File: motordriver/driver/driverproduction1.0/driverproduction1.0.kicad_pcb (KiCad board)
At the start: 4 copper layers, 28 parts

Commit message: l
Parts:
- added REF**: R_Axial_DIN0204_L3.6mm_D1.6mm_P5.08mm_Vertical, Resistor_THT:R_Axial_DIN0204_L3.6mm_D1.6mm_P5.08mm_Vertical, F.Cu at (58.7, 45.0)
- added REF**: C_Disc_D8.0mm_W5.0mm_P7.50mm, Capacitor_THT:C_Disc_D8.0mm_W5.0mm_P7.50mm, F.Cu at (73.0, 62.8)
- added REF**: C_Rect_L11.5mm_W7.8mm_P10.00mm_MKT, Capacitor_THT:C_Rect_L11.5mm_W7.8mm_P10.00mm_MKT, F.Cu at (50.6, 37.0)
- added REF**: Choke_Schaffner_RN216-04-15.5x23.0mm, Inductor_THT:Choke_Schaffner_RN216-04-15.5x23.0mm, F.Cu at (61.5, 49.8)
- added REF**: C_Radial_D16.0mm_H25.0mm_P7.50mm, Capacitor_THT:C_Radial_D16.0mm_H25.0mm_P7.50mm, F.Cu at (159.0, 43.8)
- added REF**: D_0603_1608Metric_Pad1.05x0.95mm_HandSolder, Diode_SMD:D_0603_1608Metric_Pad1.05x0.95mm_HandSolder, F.Cu at (152.5, 48.0)
- added REF**: C_Disc_D8.0mm_W5.0mm_P7.50mm, Capacitor_THT:C_Disc_D8.0mm_W5.0mm_P7.50mm, F.Cu at (73.0, 80.5)
- added REF**: D_0603_1608Metric_Pad1.05x0.95mm_HandSolder, Diode_SMD:D_0603_1608Metric_Pad1.05x0.95mm_HandSolder, F.Cu at (152.5, 57.5)
- added REF**: C_Radial_D16.0mm_H25.0mm_P7.50mm, Capacitor_THT:C_Radial_D16.0mm_H25.0mm_P7.50mm, F.Cu at (159.0, 61.8)
- moved Q** 78.4 mm to (40.6, 80.1), turned to 180 degrees
- moved Q** 77.7 mm to (40.5, 107.4), turned to 0 degrees
- moved Q** 76.6 mm to (40.6, 85.6), turned to 0 degrees
- moved Q** 76.4 mm to (40.5, 102.0), turned to 180 degrees
- moved Q** 75.7 mm to (40.6, 91.1), turned to 180 degrees
- moved Q** 75.5 mm to (40.6, 96.5), turned to 0 degrees
- moved REF** 69.5 mm to (44.9, 96.4), turned to 0 degrees
- moved REF** 69.5 mm to (44.9, 95.5), turned to 0 degrees
- moved REF** 69.1 mm to (45.2, 93.0), turned to 0 degrees
- moved REF** 69.0 mm to (45.2, 93.9), turned to 0 degrees
- moved REF** 68.7 mm to (46.3, 85.9), turned to -45 degrees
- moved REF** 68.0 mm to (46.9, 85.3), turned to -45 degrees
- moved REF** 68.0 mm to (46.6, 102.8), turned to 45 degrees
- moved REF** 67.6 mm to (47.3, 84.5), turned to -45 degrees
- moved REF** 67.4 mm to (46.5, 90.5), turned to 135 degrees
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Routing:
- net (no net): track 251.1 -> 420.2 mm
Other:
- board outline added: 180 x 100 mm

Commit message: esp32 routin
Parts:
- added REF**: C_0402_1005Metric, Capacitor_SMD:C_0402_1005Metric, F.Cu at (176.2, 83.4)
- added REF**: QFN56_7X7_EXP, esp32-s3:QFN56_7X7_EXP-L, F.Cu at (182.9, 91.4)
- added REF**: C_0402_1005Metric, Capacitor_SMD:C_0402_1005Metric, F.Cu at (179.0, 84.8)
- added REF**: C_0402_1005Metric, Capacitor_SMD:C_0402_1005Metric, F.Cu at (179.1, 83.4)
- added REF**: C_0402_1005Metric, Capacitor_SMD:C_0402_1005Metric, F.Cu at (176.7, 89.0)
- added REF**: L_0402_1005Metric, Inductor_SMD:L_0402_1005Metric, F.Cu at (176.3, 87.1)
- added REF**: C_0402_1005Metric, Capacitor_SMD:C_0402_1005Metric, F.Cu at (176.2, 84.8)
- added REF**: SOIC-8-1EP_3.9x4.9mm_P1.27mm_EP2.29x3mm, Package_SO:SOIC-8-1EP_3.9x4.9mm_P1.27mm_EP2.29x3mm, F.Cu at (196.4, 94.8)
- added REF**: C_0402_1005Metric, Capacitor_SMD:C_0402_1005Metric, F.Cu at (174.4, 86.8)
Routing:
- net (no net): track 420.2 -> 533.8 mm, vias 9 -> 16

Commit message: further updates
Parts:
- added REF**: TO-220-3_Vertical, Package_TO_SOT_THT:TO-220-3_Vertical, F.Cu at (147.2, 80.0)
- added REF**: C_0402_1005Metric, Capacitor_SMD:C_0402_1005Metric, F.Cu at (124.2, 97.1)
- added REF**: C_0603_1608Metric, Capacitor_SMD:C_0603_1608Metric, F.Cu at (152.2, 93.8)
- added REF**: QFP50P900X900X160-48N, STM32G431:QFP50P900X900X160-48N, F.Cu at (66.3, 97.3)
- added REF**: R_0402_1005Metric, Resistor_SMD:R_0402_1005Metric, F.Cu at (124.2, 99.5)
- added REF**: R_0805_2012Metric_Pad1.20x1.40mm_HandSolder, Resistor_SMD:R_0805_2012Metric_Pad1.20x1.40mm_HandSolder, F.Cu at (155.0, 82.7)
- added REF**: Crystal_SMD_3225-4Pin_3.2x2.5mm, Crystal:Crystal_SMD_3225-4Pin_3.2x2.5mm, F.Cu at (127.0, 96.0)
- added REF**: C_0603_1608Metric, Capacitor_SMD:C_0603_1608Metric, F.Cu at (152.2, 88.4)
- added REF**: C_0402_1005Metric, Capacitor_SMD:C_0402_1005Metric, F.Cu at (129.8, 96.7)
- added REF**: TO-252-3_TabPin2, Package_TO_SOT_SMD:TO-252-3_TabPin2, F.Cu at (160.0, 91.4)
- moved REF** 58.7 mm to (119.2, 98.7)
- moved REF** 58.7 mm to (119.2, 97.2)
- moved REF** 58.7 mm to (122.0, 98.7)
- moved REF** 58.7 mm to (119.3, 100.9)
- moved REF** 58.7 mm to (139.4, 108.6)
- moved REF** 58.7 mm to (117.4, 100.6)
- moved REF** 58.7 mm to (125.9, 105.2)
- moved REF** 58.7 mm to (122.0, 97.2)
- moved REF** 58.7 mm to (119.6, 102.9)
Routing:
- net (no net): track 533.8 -> 710.1 mm

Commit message: blipblub
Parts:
- added REF**: C_0402_1005Metric, Capacitor_SMD:C_0402_1005Metric, F.Cu at (122.6, 111.2)
- added REF**: C_0402_1005Metric, Capacitor_SMD:C_0402_1005Metric, F.Cu at (129.5, 99.1)
- added REF**: C_0201_0603Metric, Capacitor_SMD:C_0201_0603Metric, F.Cu at (129.1, 111.7)
- added REF**: C_0201_0603Metric, Capacitor_SMD:C_0201_0603Metric, F.Cu at (129.1, 110.8)
- moved REF** 1.53 mm to (131.2, 96.4)
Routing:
- net (no net): track 710.1 -> 873.2 mm, vias 16 -> 30

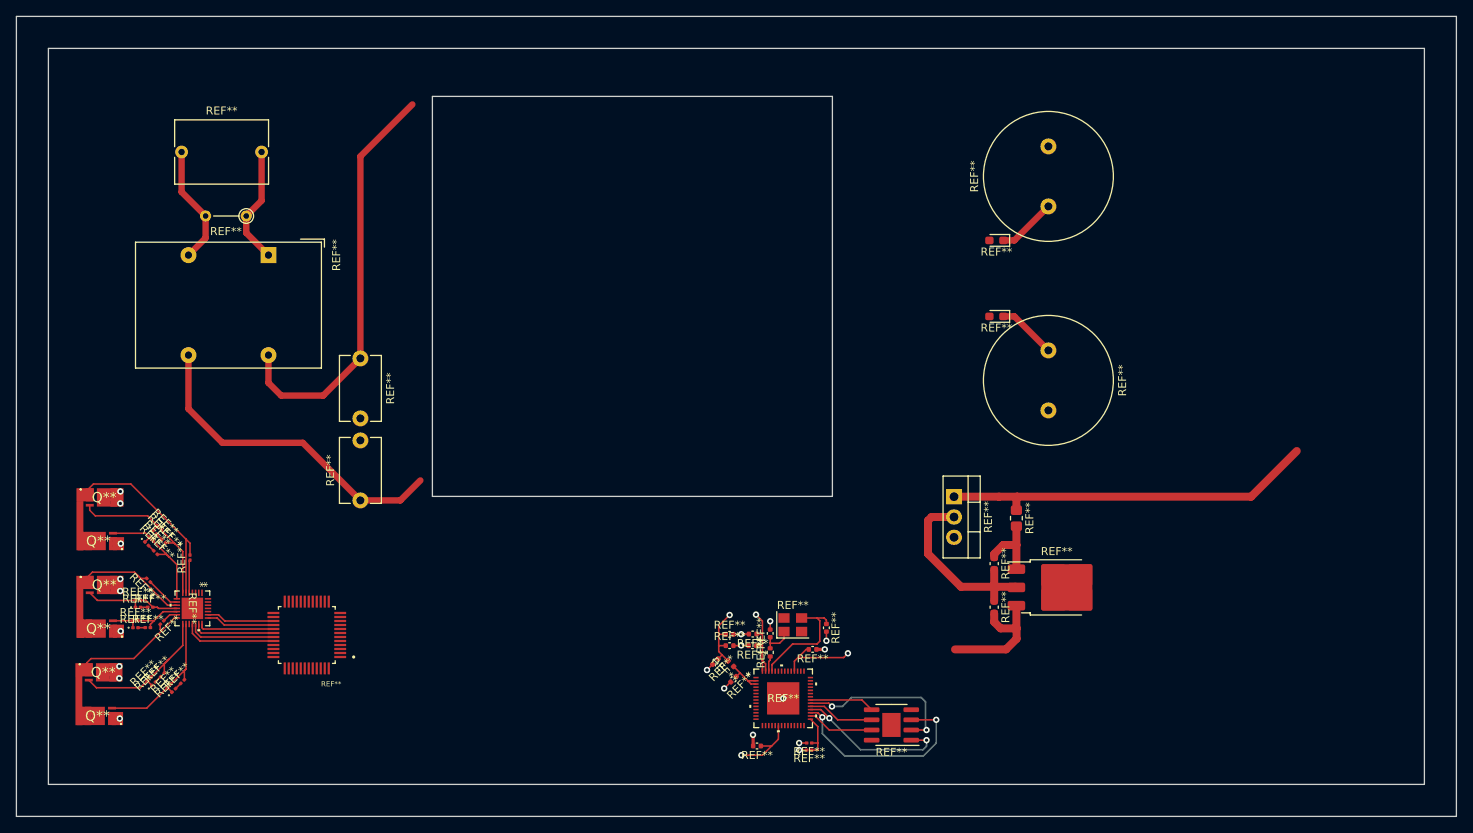
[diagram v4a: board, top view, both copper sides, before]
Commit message: reworked psuprecision
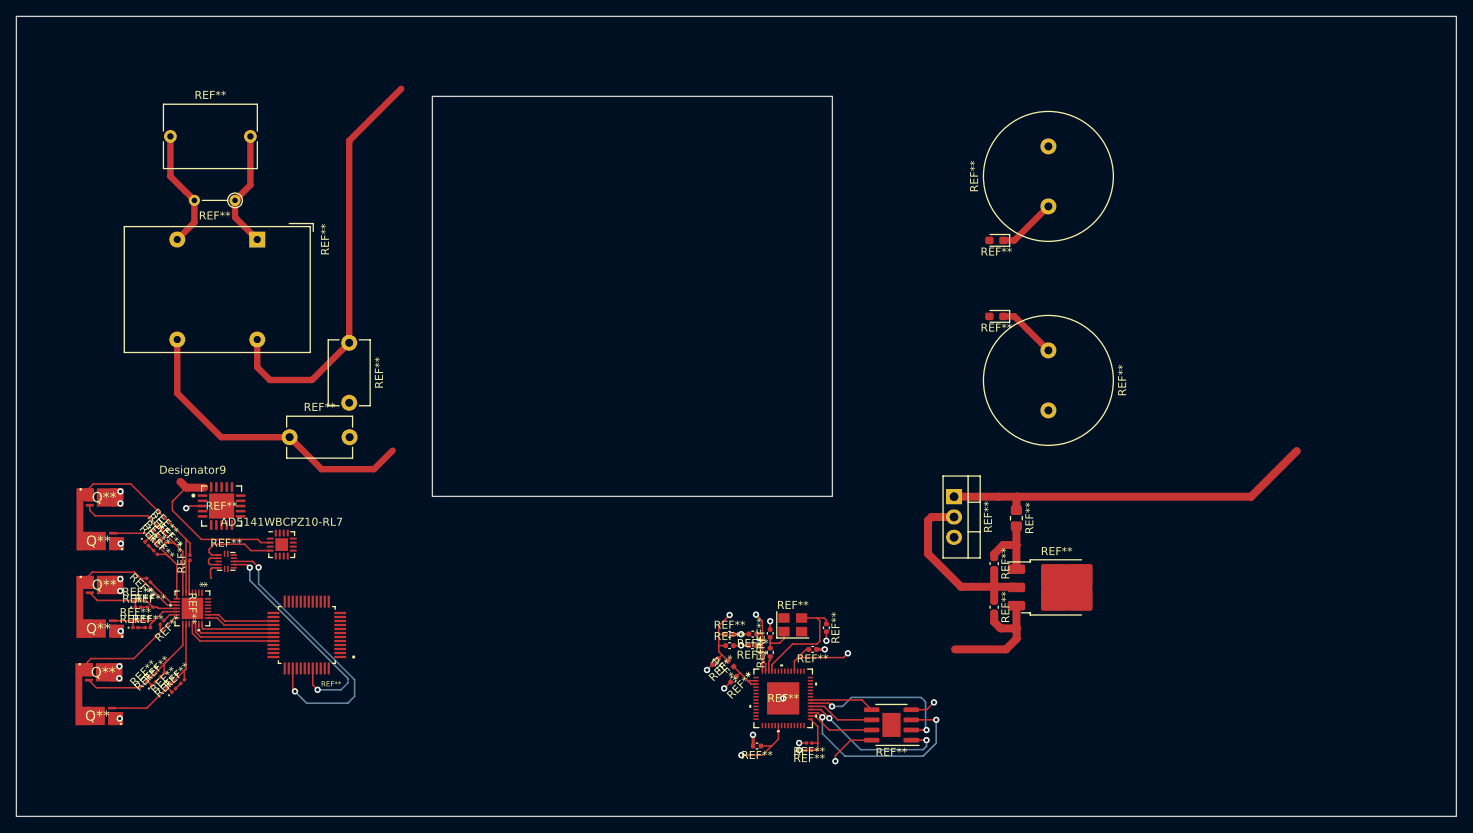
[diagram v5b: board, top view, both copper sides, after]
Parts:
- added  AD5141WBCPZ10-RL7: LFCSP-16-1EP_3x3mm_P0.5mm_EP1.6x1.6mm, Package_CSP:LFCSP-16-1EP_3x3mm_P0.5mm_EP1.6x1.6mm, F.Cu at (63.2, 86.0)
- added REF**: RGW0020A-IPC_A, ULTPS7:RGW0020A-IPC_A, F.Cu at (55.6, 81.2)
- added REF**: Texas_S-PX2QFN-14, Package_DFN_QFN:Texas_S-PX2QFN-14, F.Cu at (56.2, 88.1)
- moved REF** 11.9 mm to (64.2, 72.6), turned to 0 degrees
- moved REF** 2.40 mm to (71.6, 60.8)
- moved REF** 2.40 mm to (57.3, 43.0)
- moved REF** 2.40 mm to (49.2, 35.0)
- moved REF** 2.40 mm to (60.1, 47.9)
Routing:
- net (no net): track 873.2 -> 1011.8 mm, vias 30 -> 37
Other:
- outline, holes or cut-outs redrawn

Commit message: morewz
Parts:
- added REF**: C_0201_0603Metric, Capacitor_SMD:C_0201_0603Metric, F.Cu at (68.4, 87.9)
- added REF**: C_0201_0603Metric, Capacitor_SMD:C_0201_0603Metric, F.Cu at (70.8, 86.5)
- added REF**: C_0201_0603Metric, Capacitor_SMD:C_0201_0603Metric, F.Cu at (61.3, 82.7)
- added REF**: C_0201_0603Metric, Capacitor_SMD:C_0201_0603Metric, F.Cu at (70.0, 87.9)
- added REF**: C_0201_0603Metric, Capacitor_SMD:C_0201_0603Metric, F.Cu at (69.2, 86.5)
- added REF**: C_0201_0603Metric, Capacitor_SMD:C_0201_0603Metric, F.Cu at (61.3, 81.9)
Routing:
- net (no net): track 1011.8 -> 1062.4 mm, vias 37 -> 42

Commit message: larp
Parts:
- added IRFR9014PBF-BE3: TO-252-2, Package_TO_SOT_SMD:TO-252-2, F.Cu at (145.7, 38.6)
- added IRFR9014PBF-BE3: TO-252-2, Package_TO_SOT_SMD:TO-252-2, F.Cu at (145.8, 60.8)
- added IRLU014PBF: TO-252-2, Package_TO_SOT_SMD:TO-252-2, F.Cu at (183.9, 37.1)
- added IRLU014PBF: TO-252-2, Package_TO_SOT_SMD:TO-252-2, F.Cu at (184.6, 64.2)
- moved REF** 7.90 mm to (166.6, 59.4)
- moved REF** 7.90 mm to (166.6, 41.4)
- moved REF** 7.90 mm to (160.1, 45.7)
- moved REF** 7.90 mm to (160.1, 55.2)
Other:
- outline, holes or cut-outs redrawn

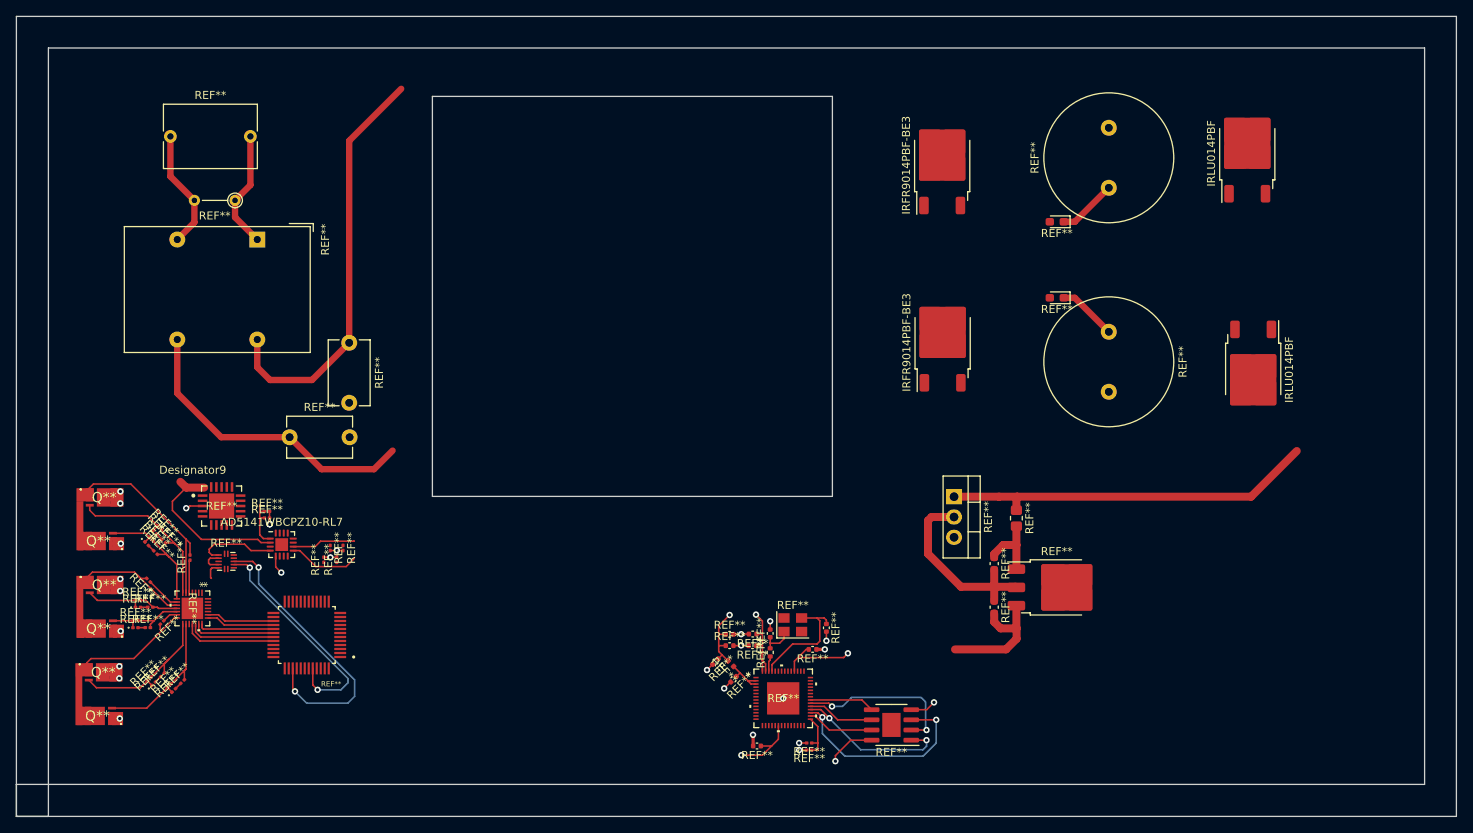
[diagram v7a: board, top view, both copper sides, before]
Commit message: Further PSU Routing
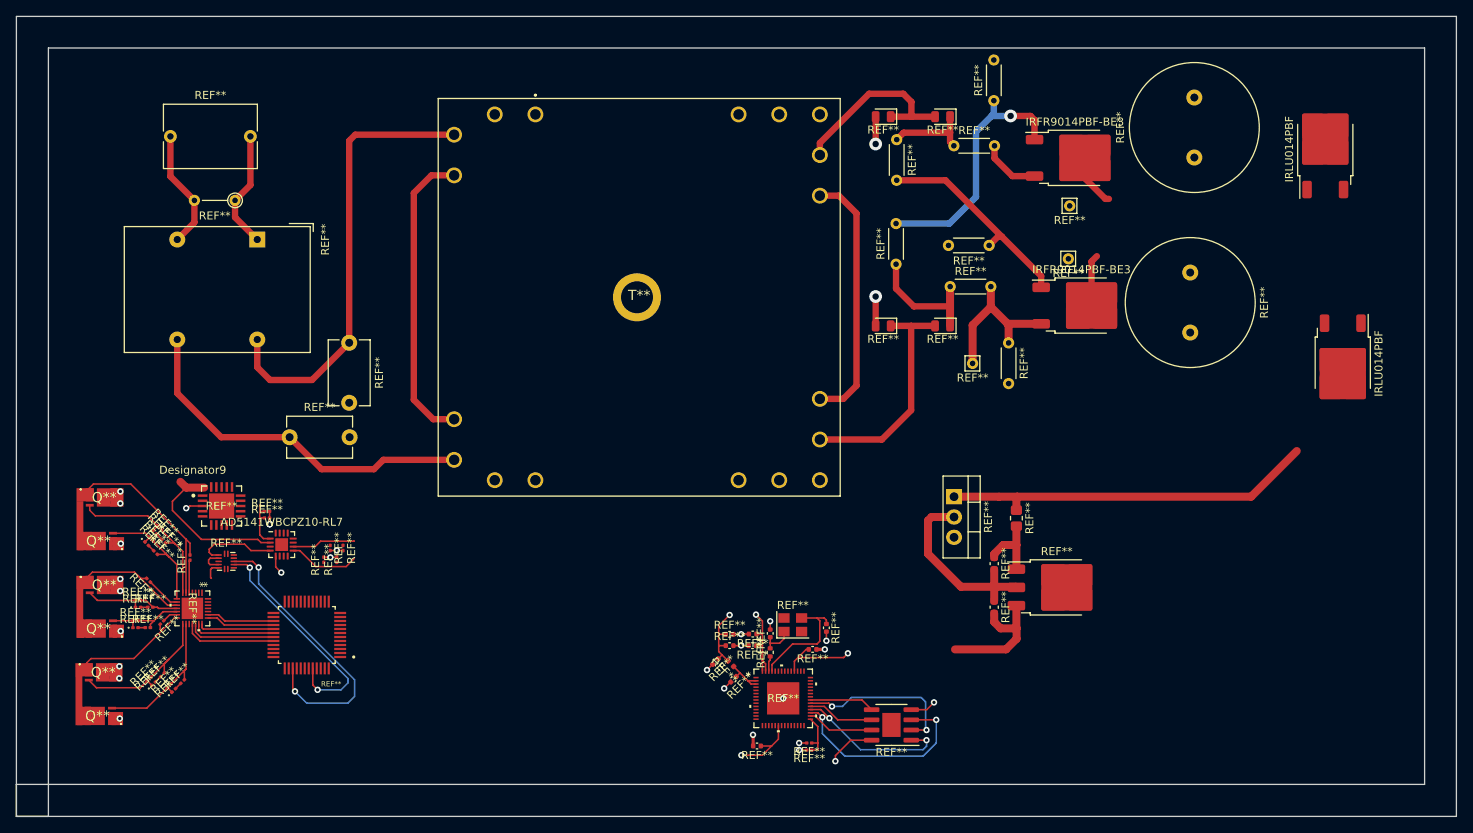
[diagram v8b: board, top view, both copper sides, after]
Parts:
- removed the REF** at (160.1, 45.7)
- removed the REF** at (160.1, 55.2)
- added REF**: Pin_D0.7mm_L6.5mm_W1.8mm_FlatFork, Connector_Pin:Pin_D0.7mm_L6.5mm_W1.8mm_FlatFork, F.Cu at (161.7, 43.7)
- added REF**: D_0805_2012Metric, Diode_SMD:D_0805_2012Metric, F.Cu at (138.3, 58.7)
- added REF**: R_Axial_DIN0204_L3.6mm_D1.6mm_P5.08mm_Horizontal, Resistor_THT:R_Axial_DIN0204_L3.6mm_D1.6mm_P5.08mm_Horizontal, F.Cu at (147.2, 36.2)
- added REF**: Pin_D0.7mm_L6.5mm_W1.8mm_FlatFork, Connector_Pin:Pin_D0.7mm_L6.5mm_W1.8mm_FlatFork, F.Cu at (161.5, 50.3)
- added REF**: R_Axial_DIN0204_L3.6mm_D1.6mm_P5.08mm_Horizontal, Resistor_THT:R_Axial_DIN0204_L3.6mm_D1.6mm_P5.08mm_Horizontal, F.Cu at (140.0, 35.4)
- added REF**: D_0805_2012Metric, Diode_SMD:D_0805_2012Metric, F.Cu at (145.8, 58.7)
- added REF**: R_Axial_DIN0204_L3.6mm_D1.6mm_P5.08mm_Horizontal, Resistor_THT:R_Axial_DIN0204_L3.6mm_D1.6mm_P5.08mm_Horizontal, F.Cu at (151.6, 48.6)
- added REF**: R_Axial_DIN0204_L3.6mm_D1.6mm_P5.08mm_Horizontal, Resistor_THT:R_Axial_DIN0204_L3.6mm_D1.6mm_P5.08mm_Horizontal, F.Cu at (140.0, 51.0)
- added REF**: R_Axial_DIN0204_L3.6mm_D1.6mm_P5.08mm_Horizontal, Resistor_THT:R_Axial_DIN0204_L3.6mm_D1.6mm_P5.08mm_Horizontal, F.Cu at (146.7, 53.8)
- added REF**: D_0805_2012Metric, Diode_SMD:D_0805_2012Metric, F.Cu at (138.3, 32.5)
- added REF**: D_0805_2012Metric, Diode_SMD:D_0805_2012Metric, F.Cu at (145.8, 32.5)
- added REF**: Pin_D0.7mm_L6.5mm_W1.8mm_FlatFork, Connector_Pin:Pin_D0.7mm_L6.5mm_W1.8mm_FlatFork, F.Cu at (149.5, 63.4)
- added REF**: R_Axial_DIN0204_L3.6mm_D1.6mm_P5.08mm_Horizontal, Resistor_THT:R_Axial_DIN0204_L3.6mm_D1.6mm_P5.08mm_Horizontal, F.Cu at (154.0, 60.8)
- added REF**: R_Axial_DIN0204_L3.6mm_D1.6mm_P5.08mm_Horizontal, Resistor_THT:R_Axial_DIN0204_L3.6mm_D1.6mm_P5.08mm_Horizontal, F.Cu at (152.2, 30.5)
- added T**: 70020K, tordial transformer:70020K, F.Cu at (94.9, 32.2)
- moved IRFR9014PBF-BE3 18.0 mm to (163.1, 56.1), turned to 0 degrees
- moved IRFR9014PBF-BE3 16.6 mm to (162.3, 37.7), turned to 0 degrees
- moved REF** 12.6 mm to (176.7, 52.0)
- moved REF** 11.3 mm to (177.2, 37.6)
- moved IRLU014PBF 11.2 mm to (195.8, 63.4)
- moved IRLU014PBF 9.76 mm to (193.6, 36.6)
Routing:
- net (no net): track 1062.4 -> 1383.2 mm, vias 42 -> 45
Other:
- outline, holes or cut-outs redrawn
